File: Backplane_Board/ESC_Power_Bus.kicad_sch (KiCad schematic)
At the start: 23 parts, among them J3 Conn_01x02_Pin, Q2 ZXMN3A14F, SW2 SW_DPST_x2

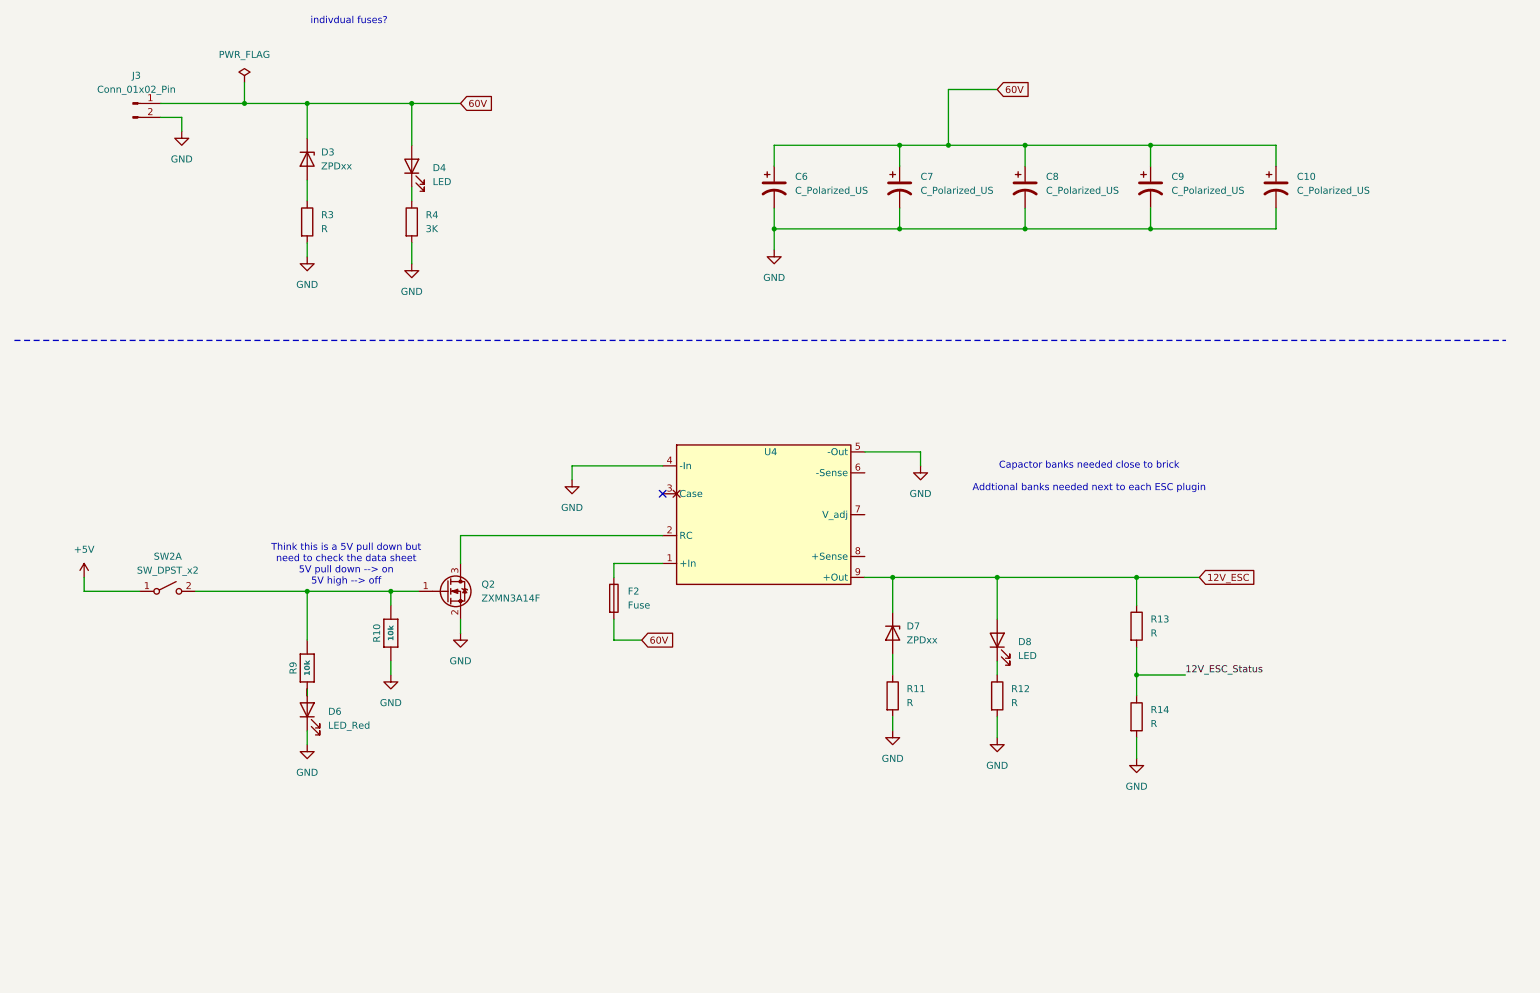
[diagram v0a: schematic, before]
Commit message: added ad converter
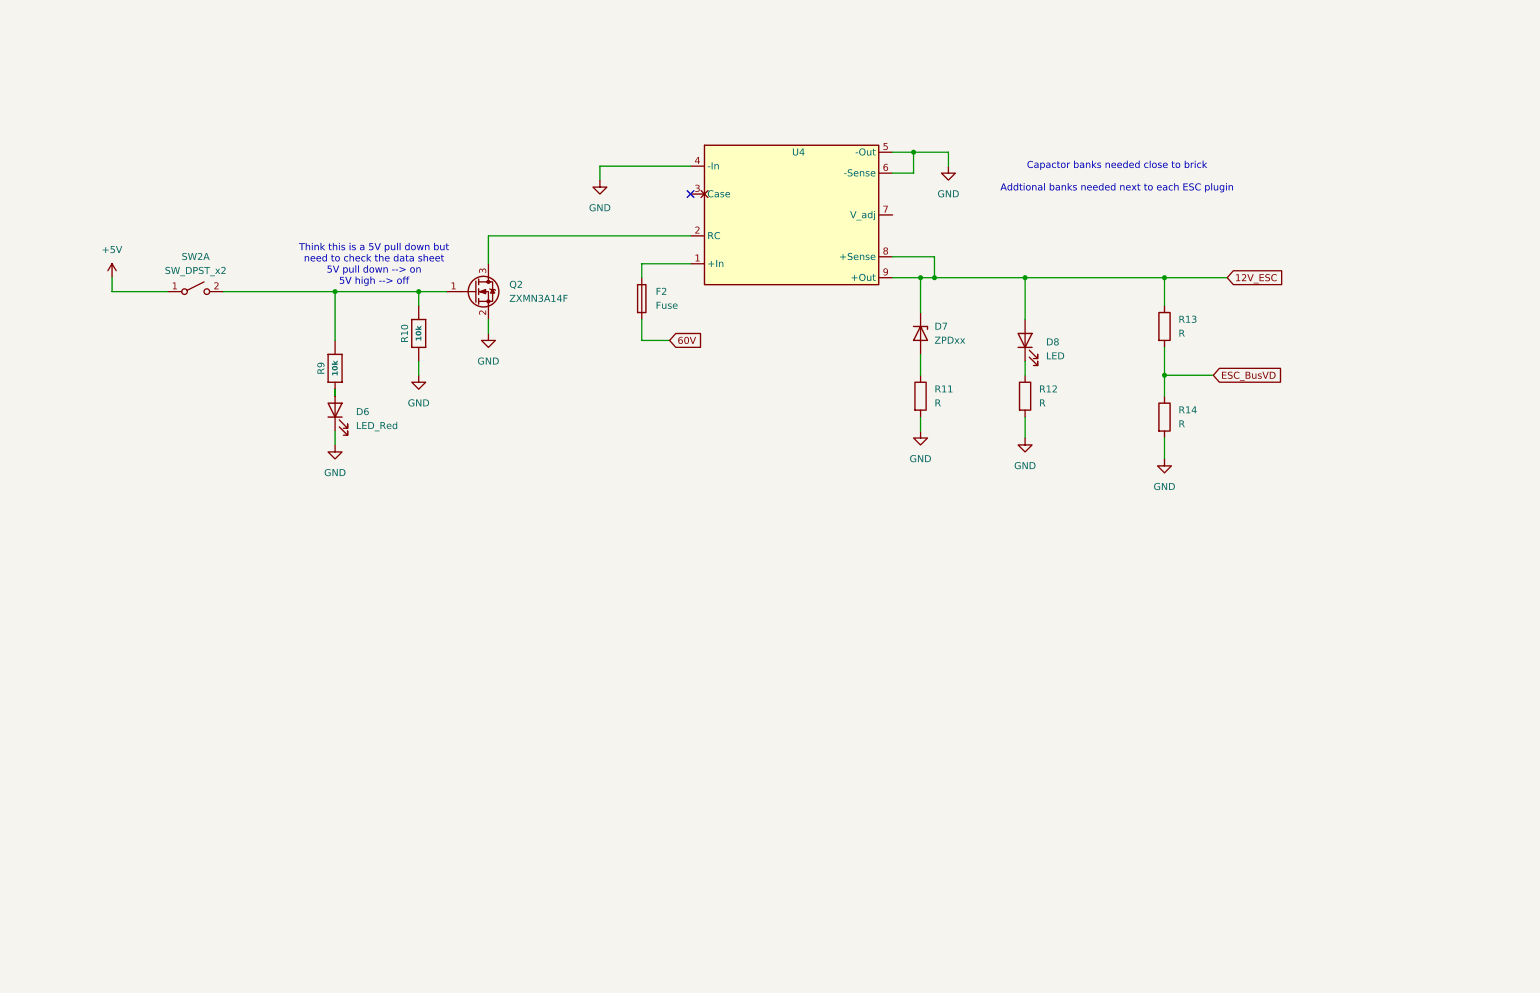
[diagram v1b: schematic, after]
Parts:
- removed C10, C6, C7, C8, C9: C_Polarized_US, symbol Device:C_Polarized_US
- removed D3: ZPDxx, Diode_THT:D_DO-35_SOD27_P10.16mm_Horizontal, symbol Diode:ZPDxx
- removed D4: LED, symbol Device:LED
- removed J3: Conn_01x02_Pin, symbol Connector:Conn_01x02_Pin
- removed R3: R, symbol Device:R
- removed R4: 3K, symbol Device:R
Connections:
- net 12V_ESC: now also U4.8 (+Sense)
- net GND: now also U4.6 (-Sense)
- net 12V_ESC_Status renamed ESC_BusVD
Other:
- note removed: "indivdual fuses?"
- moved on the sheet: D6, D7, D8, F2, Q2, R10, R11, R12, R13, R14, R9, SW2A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

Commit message: add rerevised esc board and rough backplane schmatic
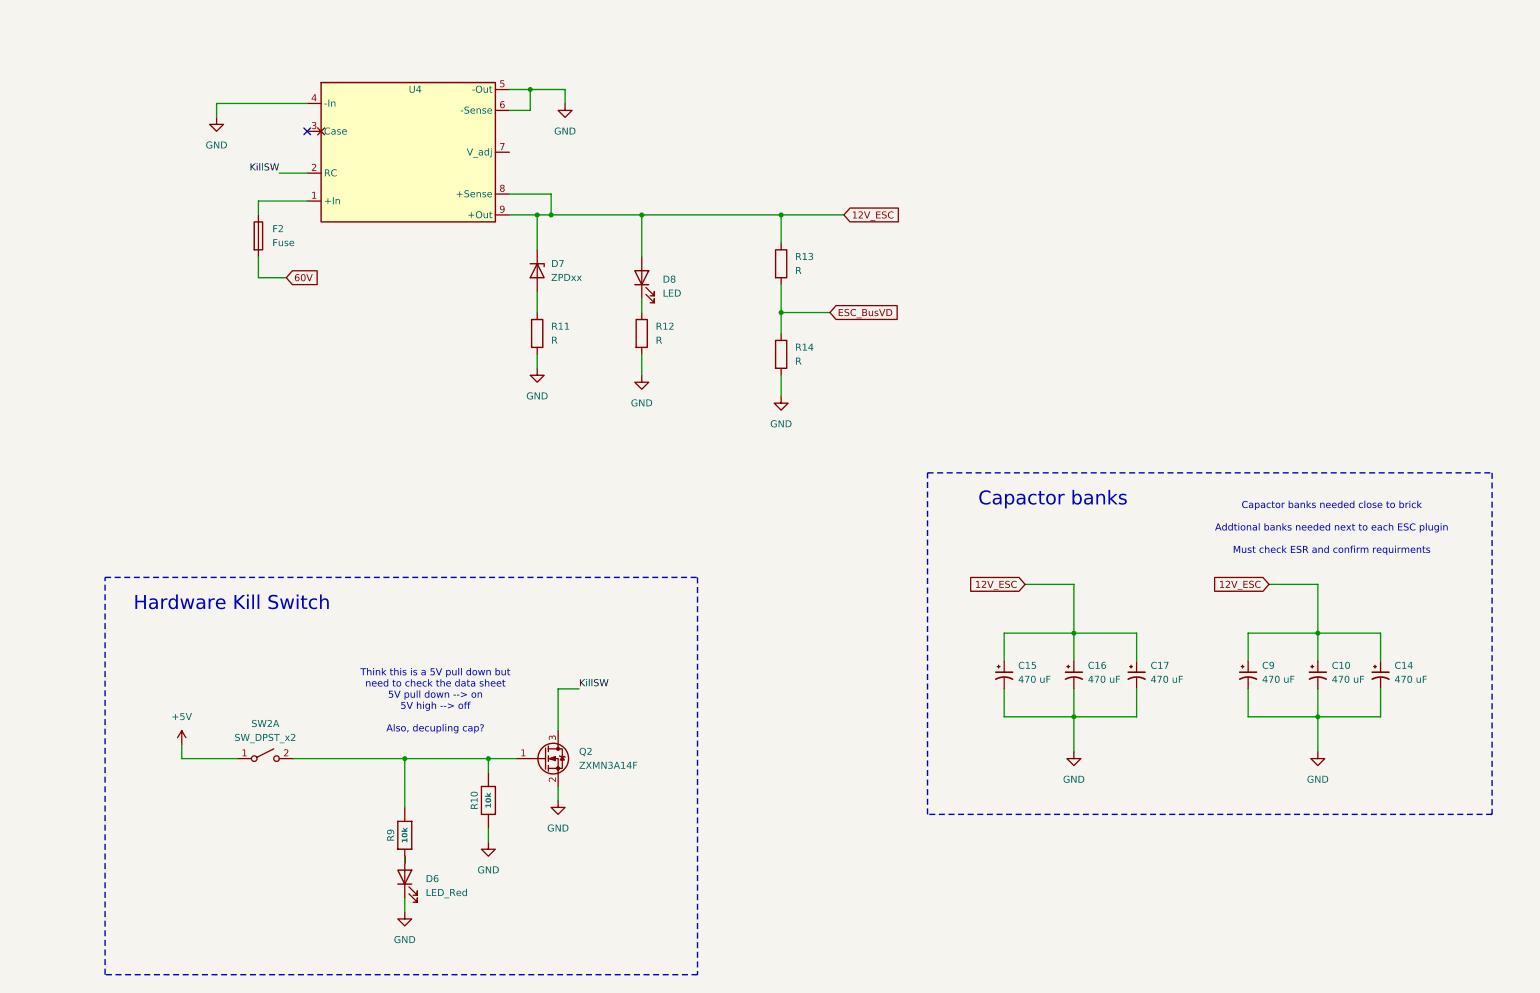
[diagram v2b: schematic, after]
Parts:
- added C10, C14, C15, C16, C17, C9: 470 uF, 470UF CAP:CAP_EEHZU1V471V, symbol Device:C_Polarized_Small_US
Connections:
- net 12V_ESC: now also C10.1, C14.1, C15.1, C16.1, C17.1, C9.1
- net GND: now also C10.2, C14.2, C15.2, C16.2, C17.2, C9.2
- net KillSW: now reaches Q2.3 (D), U4.2 (RC)
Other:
- note added: "Capactor banks"
- note added: "Capactor banks needed close to brick Addtional banks needed next to each ESC plugin Must check ESR and confirm requirments"
- note added: "Hardware Kill Switch"
- note added: "Think this is a 5V pull down but need to check the data sheet 5V pull down --> on 5V high --> off Also, decupling cap?"
- note removed: "Capactor banks needed close to brick Addtional banks needed next to each ESC plugin"
- note removed: "Think this is a 5V pull down but need to check the data sheet 5V pull down --> on 5V high --> off"
- company: (none) -> Cabrillo Robtics
- title: (none) -> ESC Power Bus
- moved on the sheet: D6, D7, D8, F2, Q2, R10, R11, R12, R13, R14, R9, SW2A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

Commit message: backup before heavy revtion
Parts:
- removed C14: 470 uF, 470UF CAP:CAP_EEHZU1V471V, symbol Device:C_Polarized_Small_US
- added C11: 2.2uF+/35V+, Capacitor_SMD:C_0805_2012Metric, symbol Adafruit MOSFET Driver STEMMA Breakout-eagle-import:CAP_CERAMIC0805-NOOUTLINE
- added C12: 470 uF, 470UF CAP:CAP_EEHZU1V471V, symbol Device:C_Polarized_Small_US
- added C13, C14, C18, C19: 22uF, C2012X5R1V226M125AC:CAPC2012X145N, symbol C2012X5R1V226M125AC:C2012X5R1V226M125AC
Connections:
- net 12V_ESC: now also C12.1, C13.2, C14.2, C18.2, C19.2
- net GND: now also C11.2, C12.2, C13.1, C14.1, C18.1, C19.1
- net KillSW: now also C11.1
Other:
- moved on the sheet: C15, C16, C17, D7, D8, F2, R11, R12, R13, R14, U4

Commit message: back plane board ready for review
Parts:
- removed C11: 2.2uF+/35V+, Capacitor_SMD:C_0805_2012Metric, symbol Adafruit MOSFET Driver STEMMA Breakout-eagle-import:CAP_CERAMIC0805-NOOUTLINE
- removed D6: LED_Red, LED_SMD:LED_0603_1608Metric, symbol Device:LED
- removed Q2: ZXMN3A14F, Package_TO_SOT_SMD:SOT-23, symbol Transistor_FET:ZXMN3A14F
- removed R10, R9: 10k, Resistor_SMD:R_0805_2012Metric, symbol Adafruit MOSFET Driver STEMMA Breakout-eagle-import:RESISTOR_0603_NOOUT
- added J21: Conn_01x02_Pin, symbol Connector:Conn_01x02_Pin
- R12: value R -> 10k
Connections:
- net +5V is gone; now on net KillSW: SW2.1 (A)
- net GND: now also SW2.2 (B), J21.2 (Pin_2)
- net KillSW: now also J21.1 (Pin_1)
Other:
- note added: "12V ESC Power Bus"
- note added: "3V3 VD?"
- note added: "Delete or DNP?"
- note added: "Kill Switch Saftey Bypass"
- note added: "TODO: Make sure the power bricks have OCP, if so remove fuses"
- note added: "The ESR is currently goint to be under the 5mOhm. To Fix this, we need to either use smaller qty of larger caps or put some caps in series. Also the small ciramic capactors do not have a specfied ESR."
- note added: "The data sheet says: - recommended capactive load 3000uF on the output of this bus. - ESR is important and oppration is garented with a varafied ESR value greater than 5mOhm across the output conections - Should use both ceramic and electrostatic capactors"
- note added: "When RC is tied to 0V the brick turns on. This pun will be tied to a magnetic read switch. We need to make sure that this switch is stable."
- note removed: "Think this is a 5V pull down but need to check the data sheet 5V pull down --> on 5V high --> off Also, decupling cap?"
- moved on the sheet: C10, C12, C13, C14, C15, C16, C17, C18, C19, C9, SW2A

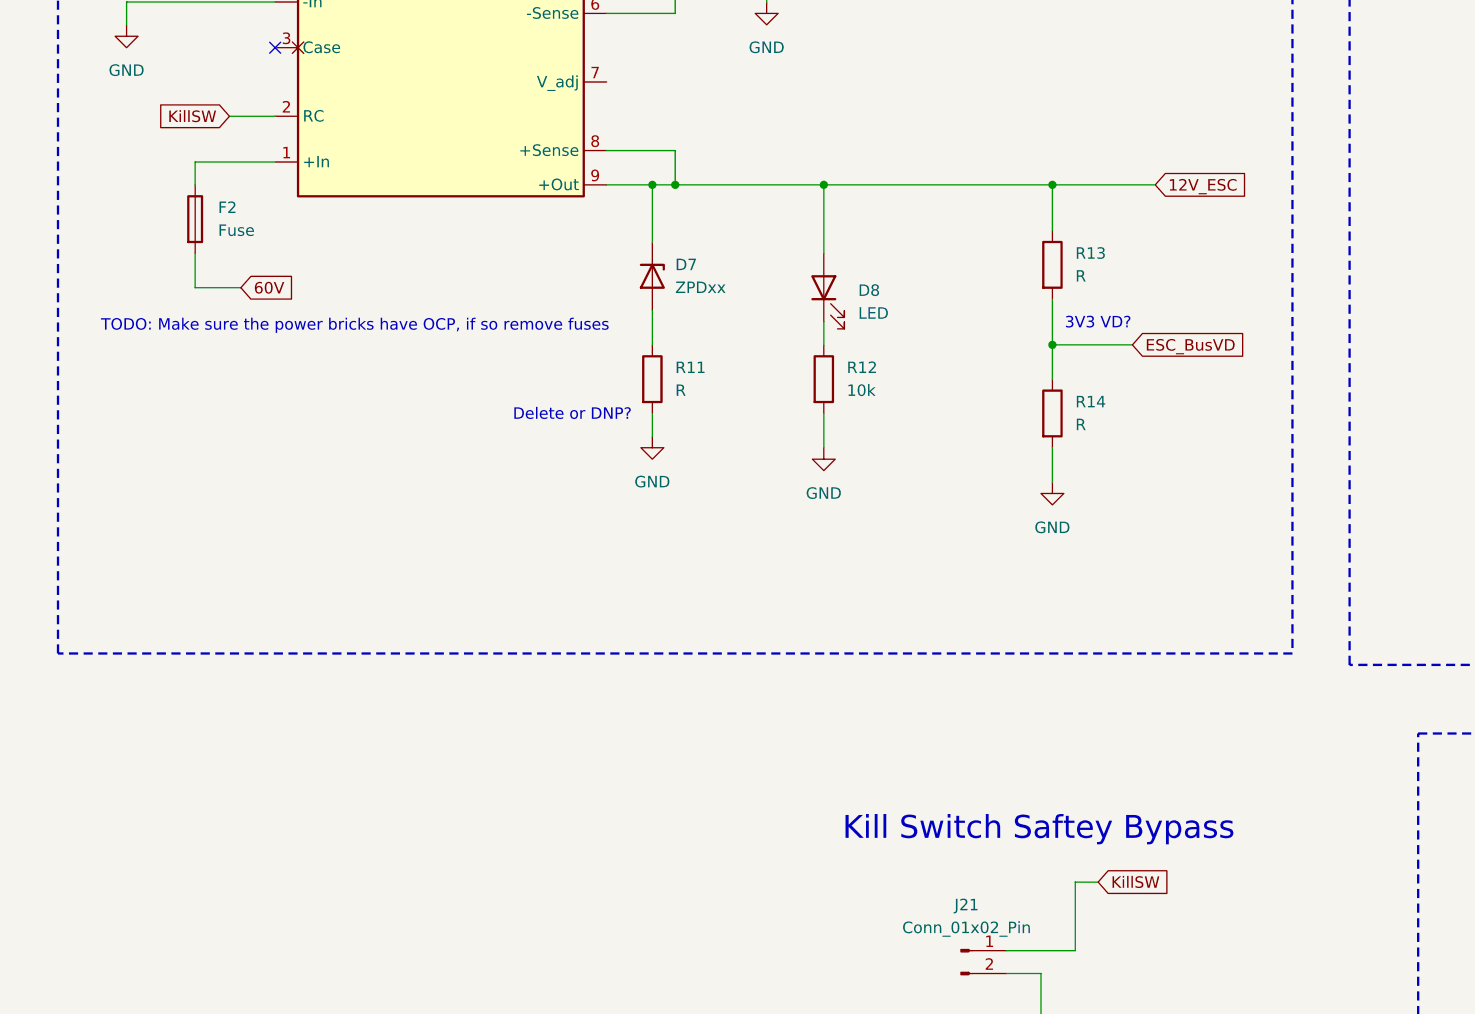
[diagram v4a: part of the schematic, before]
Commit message: adding dull power path ic into sepret exption board
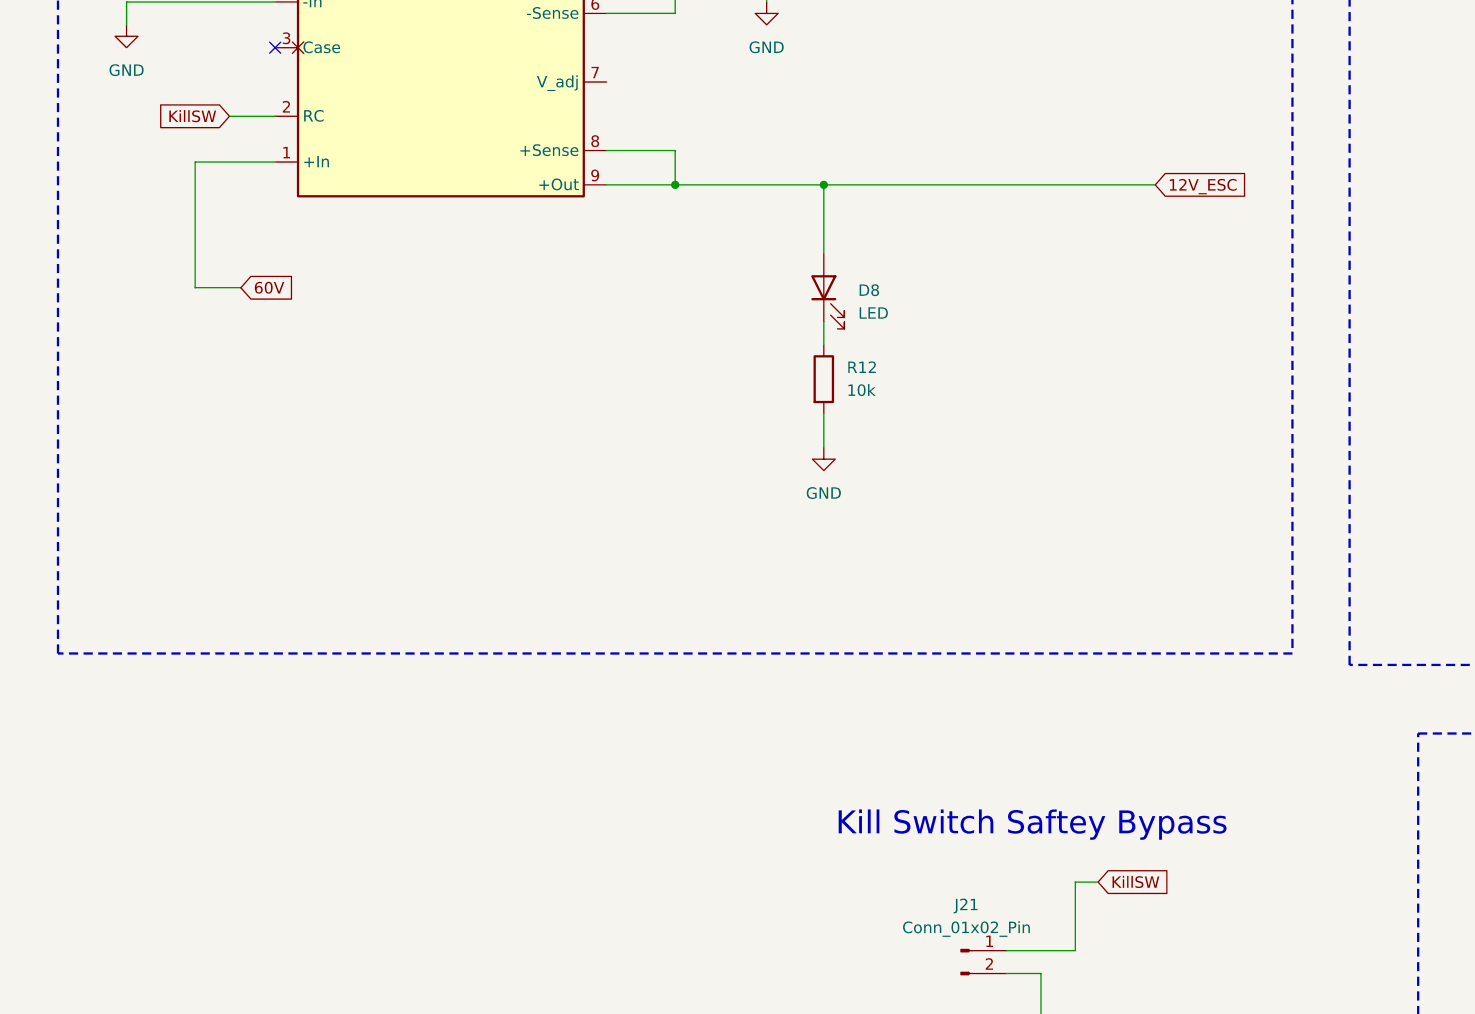
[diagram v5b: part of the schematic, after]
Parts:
- removed D7: ZPDxx, Diode_THT:D_DO-35_SOD27_P10.16mm_Horizontal, symbol Diode:ZPDxx
- removed F2: Fuse, symbol Device:Fuse
- removed R11, R13, R14: R, symbol Device:R
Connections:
- net 60V: now also U4.1 (+In)
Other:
- note removed: "3V3 VD?"
- note removed: "Delete or DNP?"
- note removed: "TODO: Make sure the power bricks have OCP, if so remove fuses"

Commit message: from desing review 1
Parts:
- removed C10, C12, C16, C17: 470 uF, 470UF CAP:CAP_EEHZU1V471V, symbol Device:C_Polarized_Small_US
- added C1: 680u, symbol Device:C_Polarized_Small_US
- added R11, R13, R14, R16: 330m, footprints:RES_KDV12_OHM-L, symbol Device:R_US
- added R3, R9: DNP, symbol Device:R
- C15, C9: value 470 uF -> 680u; footprint 470UF CAP:CAP_EEHZU1V471V -> (none)
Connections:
- net 12V_ESC: now also C1.1, R11.1, R13.1, R14.1, R16.1, R9.2; no longer C13.2, C14.2, C18.2, C19.2
- net GND: now also C1.2, R3.1
- net at U4.7 (V_adj): now also R3.2, R9.1
- new net: C14.2, R13.2
- new net: C19.2, R16.2
- new net: C13.2, R11.2
- new net: C18.2, R14.2
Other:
- note added: "- 3/16+4/R=1/5 --> R = 320mOhm = 0.32Ohm (tempture controlled persistion) - We must add series resistors inline with the ciramice caps inorder to get with in the threshold of 5mOhm. -R_total = (3/16 + 4/320)^-1 = 5.0m --> OK! We could increase the value thses resistors a little bit to stay a safe difference above the 5m."
- note added: "- C_total = 3*680 + 4*22 = 2128u - Think this is close enoguh to the specfied value of 333u"
- note added: "Ceramic"
- note added: "Electrolytic"
- note removed: "Capactor banks needed close to brick Addtional banks needed next to each ESC plugin Must check ESR and confirm requirments"
- note removed: "The ESR is currently goint to be under the 5mOhm. To Fix this, we need to either use smaller qty of larger caps or put some caps in series. Also the small ciramic capactors do not have a specfied ESR."
- moved on the sheet: C13, C14, C15, C18, C19, J21, SW2A
